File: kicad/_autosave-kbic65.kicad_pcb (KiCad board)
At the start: 2 copper layers, 313.3 x 123.8 mm, 154 parts, among them U1 ProMicro

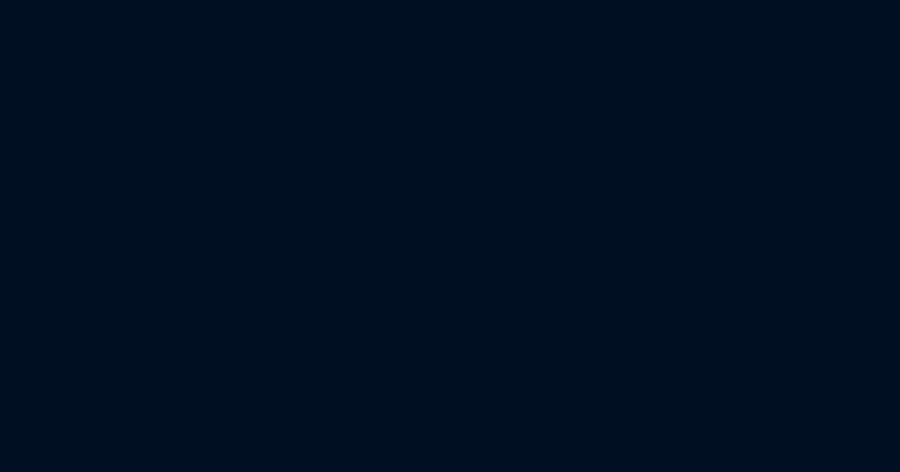
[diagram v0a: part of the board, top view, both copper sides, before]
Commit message: Thinking about plate size, added current state of pcb
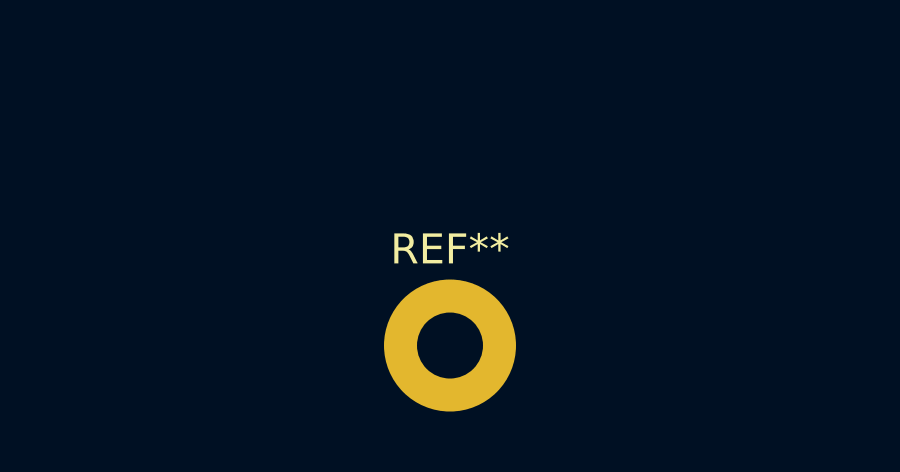
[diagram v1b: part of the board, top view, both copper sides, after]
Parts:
- added REF**: MountingHole_2.2mm_M2_Pad, MountingHole:MountingHole_2.2mm_M2_Pad, F.Cu at (158.0, 182.6)
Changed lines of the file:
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@@
     (tracks 993)
     (zones 0)
-    (modules 154)
+    (modules 155)
     (nets 95)
   )
@@
     (add_net ROW8)
   )
+  (module MountingHole:MountingHole_2.2mm_M2_Pad (layer F.Cu)
+    (at 157.95625 182.5625)
+    (descr "Mounting Hole 2.2mm, M2")
+    (tags "mounting hole 2.2mm m2")
+    (attr virtual)
+    (fp_text reference REF** (at 0 -3.2) (layer F.SilkS)
+      (effects (font (size 1 1) (thickness 0.15)))
+    )
+    (fp_text value MountingHole_2.2mm_M2_Pad (at 0 3.2) (layer F.Fab)
+      (effects (font (size 1 1) (thickness 0.15)))
+    )
+    (fp_text user %R (at 0.3 0) (layer F.Fab)
+      (effects (font (size 1 1) (thickness 0.15)))
+    )
+    (fp_circle (center 0 0) (end 2.2 0) (layer Cmts.User) (width 0.15))
+    (fp_circle (center 0 0) (end 2.45 0) (layer F.CrtYd) (width 0.05))
+    (pad 1 thru_hole circle (at 0 0) (size 4.4 4.4) (drill 2.2) (layers *.Cu *.Mask))
+  )
   (module KBIC-Parts:MountingHole_5mm_KB (layer F.Cu)

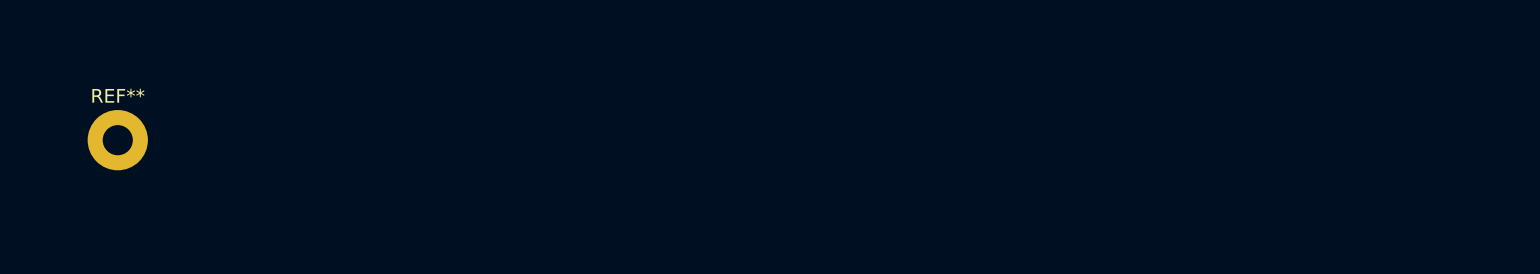
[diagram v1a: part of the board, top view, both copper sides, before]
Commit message: Drew first version of plate
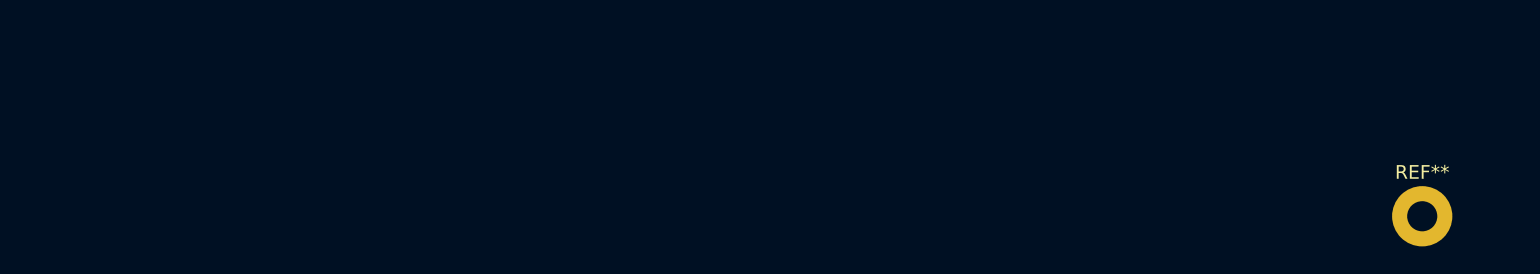
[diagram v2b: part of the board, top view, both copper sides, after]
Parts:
- moved REF** 95.4 mm to (253.2, 188.1)
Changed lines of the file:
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@@
     (pad_to_mask_clearance 0)
     (aux_axis_origin 0 0)
-    (visible_elements 7FFFFFFF)
+    (visible_elements 7FFFEFFF)
     (pcbplotparams
       (layerselection 0x010fc_ffffffff)
@@
   )
   (module MountingHole:MountingHole_2.2mm_M2_Pad (layer F.Cu)
-    (at 157.95625 182.5625)
+    (at 253.20625 188.11875)
     (descr "Mounting Hole 2.2mm, M2")
     (tags "mounting hole 2.2mm m2")
